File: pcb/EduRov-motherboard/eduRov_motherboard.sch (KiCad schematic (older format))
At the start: 25 parts, among them P101 Battery connector, P102 Ext press, P103 Ext press, P104 Ext press, P105 Ch LED, Q101 IRL540NPBF

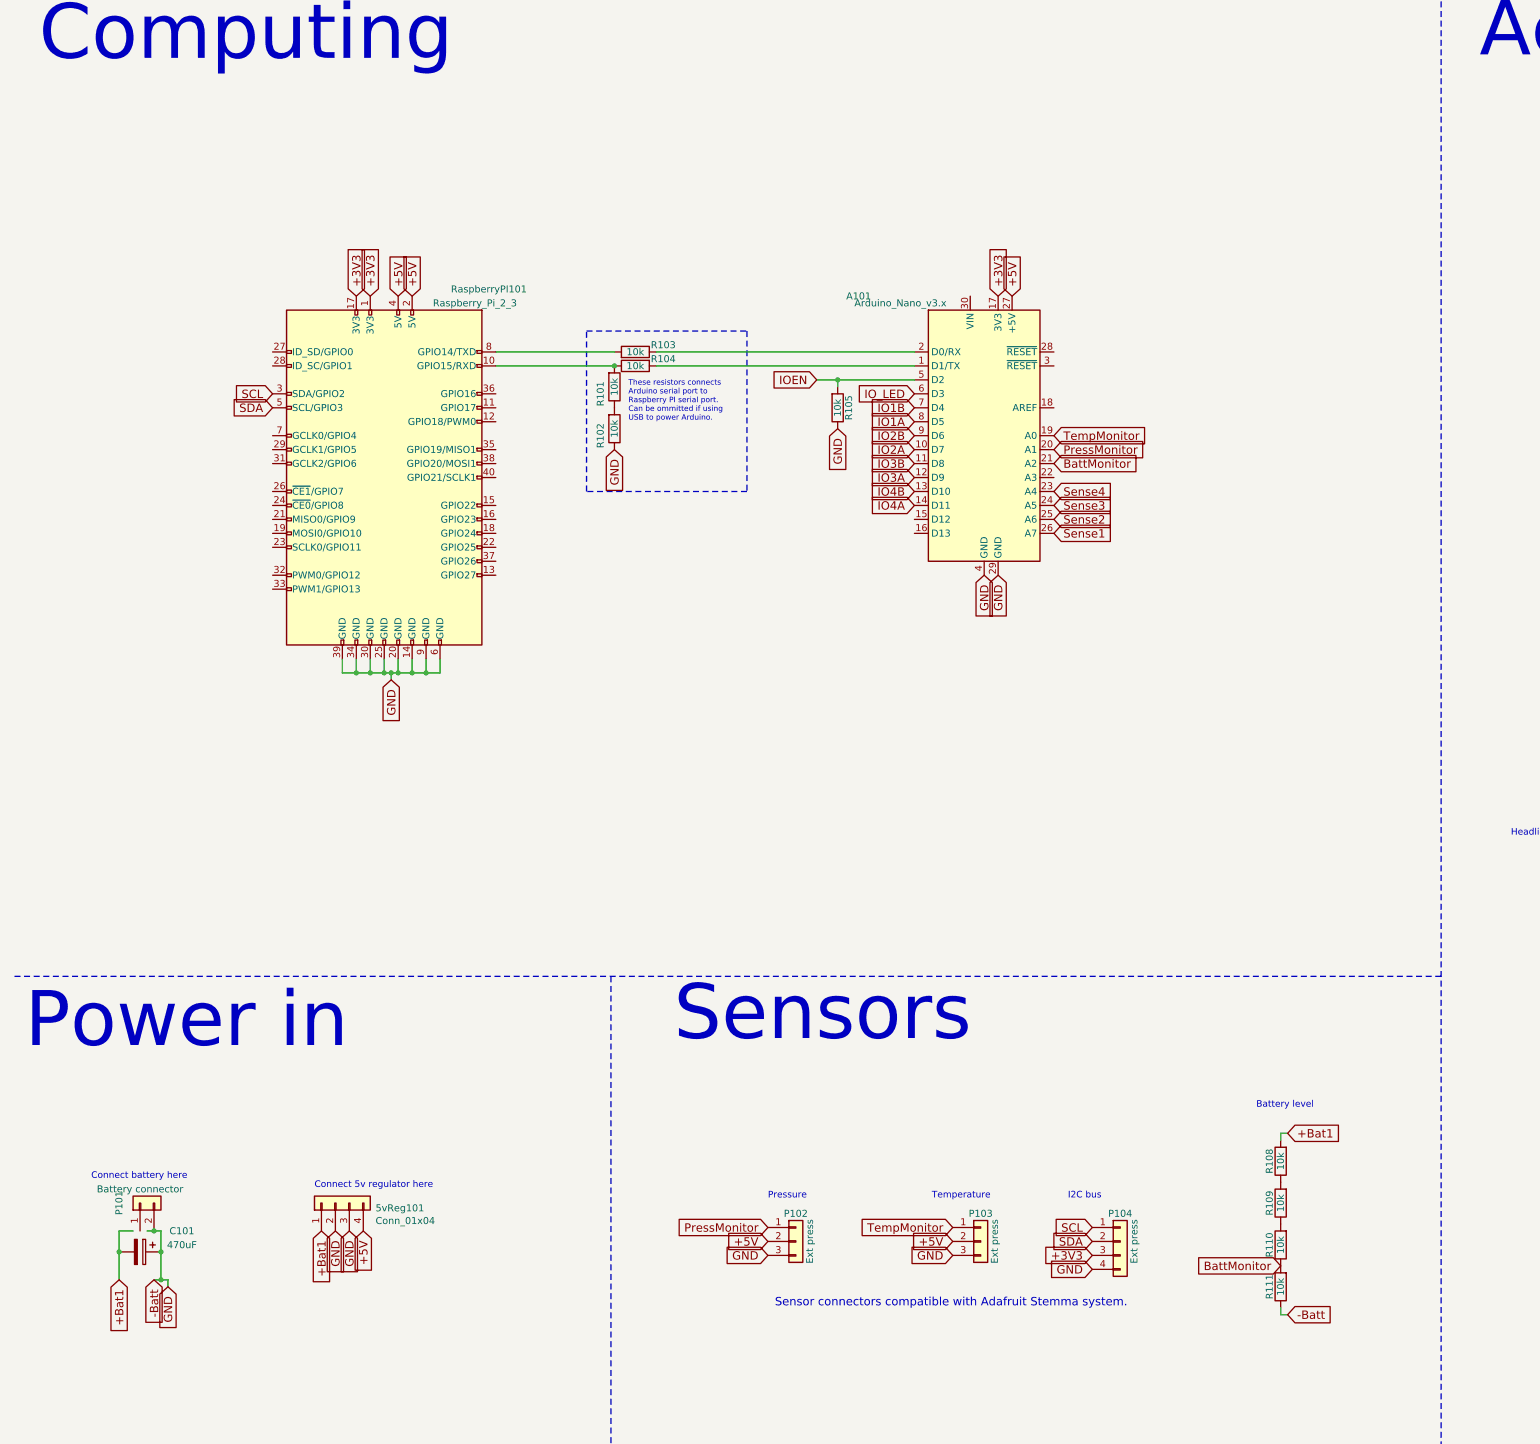
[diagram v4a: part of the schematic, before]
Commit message: Start adding digikey ordering info to all components.
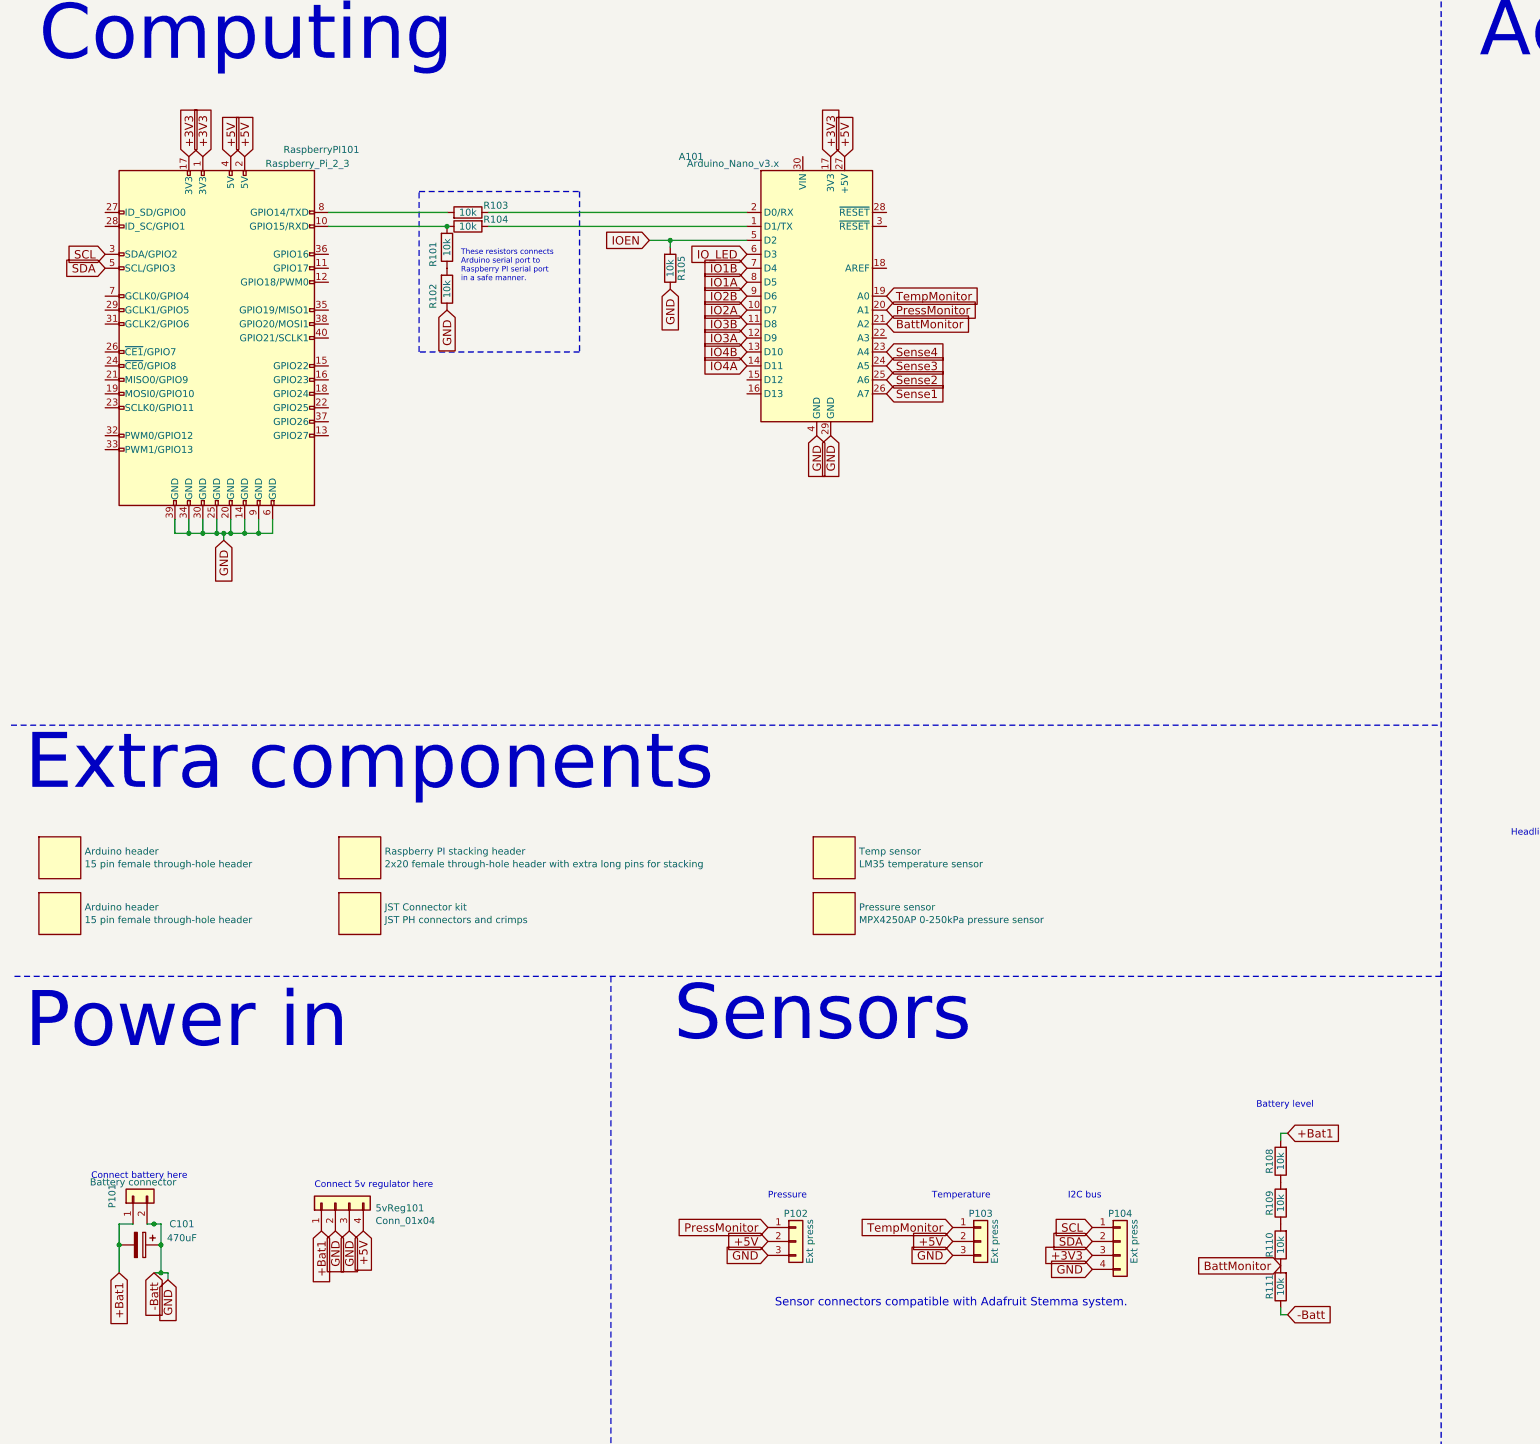
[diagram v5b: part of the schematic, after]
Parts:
- added U1, U2: Arduino header, symbol Edurov:Generic
- added U3: Raspberry PI stacking header, symbol Edurov:Generic
- added U4: Temp sensor, symbol Edurov:Generic
- added U5: Pressure sensor, symbol Edurov:Generic
- added U?: JST Connector kit, symbol Edurov:Generic
- 5vReg101: Description (none) -> Iflight micro 30V->5V regulator, 2.5A; Elefun reference (none) -> IF-A006172; Part number (none) -> Micro
- C101: Description (none) -> 470uF, 20%, 50V, 5mm pitch; Digikey reference (none) -> 493-12789-1-ND; Part number (none) -> UVR1H471MHD1TO
- C102: Description (none) -> 100nF, 50V X7R, 2.5mm pitch; Digikey reference (none) -> 445-FG18X7R1H104KNT00-ND; Part number (none) -> FG18X7R1H104KNT00
- P101: Description (none) -> 2-position terminal block, 12-30 AWG, 5mm pitch; Digikey reference (none) -> 732-10955-ND; Part number (none) -> 691137710002
- R101, R102, R103, R104, R105, R108, R109, R110, R111, R112: Description (none) -> 10k Ohm, 1/4W, 5%; Digikey reference (none) -> CF14JT10K0CT-ND; Part number (none) -> CF14JT10K0
- RaspberryPI101: Description (none) -> Raspberry PI 3 or 4; DigiKey reference (none) -> 1690-RASPBERRYPI4B/4GB-ND; Part number (none) -> Raspberry PI 3 or 4
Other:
- note added: "Extra components"
- note added: "These resistors connects \nArduino serial port to \nRaspberry PI serial port \nin a safe manner."
- note removed: "These resistors connects \nArduino serial port to \nRaspberry PI serial port.\nCan be ommitted if using \nUSB to power Arduino."
- moved on the sheet: A101, C101, P101, R101, R102, R103, R104, R105, RaspberryPI101

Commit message: Add rest of component descriptions.
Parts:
- added U10, U14, U18, U22: Nut, symbol Edurov:Generic
- added U11, U13, U15, U17, U19, U21, U23, U9: Ferrules for motor cables, symbol Edurov:Generic
- added U12, U16, U20, U24: Standoff, symbol Edurov:Generic
- added U6: Sense hat, symbol Edurov:Generic
- added U7: Camera, symbol Edurov:Generic
- 2Pscrew101, 2Pscrew102, 2Pscrew103, 2Pscrew104: Description (none) -> 2-position terminal block, 12-30 AWG, 5mm pitch; Digikey reference (none) -> 732-10955-ND; Manufacturer (none) -> Wurth; Part number (none) -> 691137710002
- 5vReg101: Manufacturer (none) -> IFlight
- A101: Description (none) -> ARDUINO NANO EVERY with headers; Digikey reference (none) -> 1050-ABX00033-ND; Manufacturer (none) -> Arduino; Part number (none) -> ABX00033
- C101: Manufacturer (none) -> Nichicon
- C102: Manufacturer (none) -> TDK Corporation
- P101: Manufacturer (none) -> Wurth
- P102, P103: Description (none) -> 2.5mm pitch 3-pin receptacle, JST PH; Manufacturer (none) -> JST; Part number (none) -> PHR-3
- P104, P105: Description (none) -> 2.5mm pitch 4-pin receptacle, JST PH; Manufacturer (none) -> JST; Part number (none) -> PHR-4
- Q101: Description (none) -> MOSFET, >2A, Vgth = 2V; Digikey reference (none) -> IRL540NPBF-ND; Manufacturer (none) -> Infineon Technologies; Part number (none) -> IRL540NPBF
- R101, R102, R103, R104, R105, R108, R109, R110, R111, R112: Manufacturer (none) -> Stackpole Electronics Inc
- RaspberryPI101: DigiKey reference 1690-RASPBERRYPI4B/4GB-ND -> (none); Digikey reference (none) -> 1690-RASPBERRYPI4B/4GB-ND; Manufacturer (none) -> Raspberry Pi
- U1, U2: Manufacturer (none) -> Samtec Inc.
- U3: Manufacturer (none) -> Adafruit Industries LLC
- U4: Manufacturer (none) -> Texas Instruments
- U5: Manufacturer (none) -> NXP
- U8: renamed from U?; Manufacturer (none) -> DFRobot
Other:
- moved on the sheet: 5vReg101, C101, P101, P102, P103, P104, R108, R109, R110, R111
